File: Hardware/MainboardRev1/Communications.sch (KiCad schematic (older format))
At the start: 12 parts, among them J8 915MHz_SMA, U17 ublox_max-m8q, U18 RFM69HCW

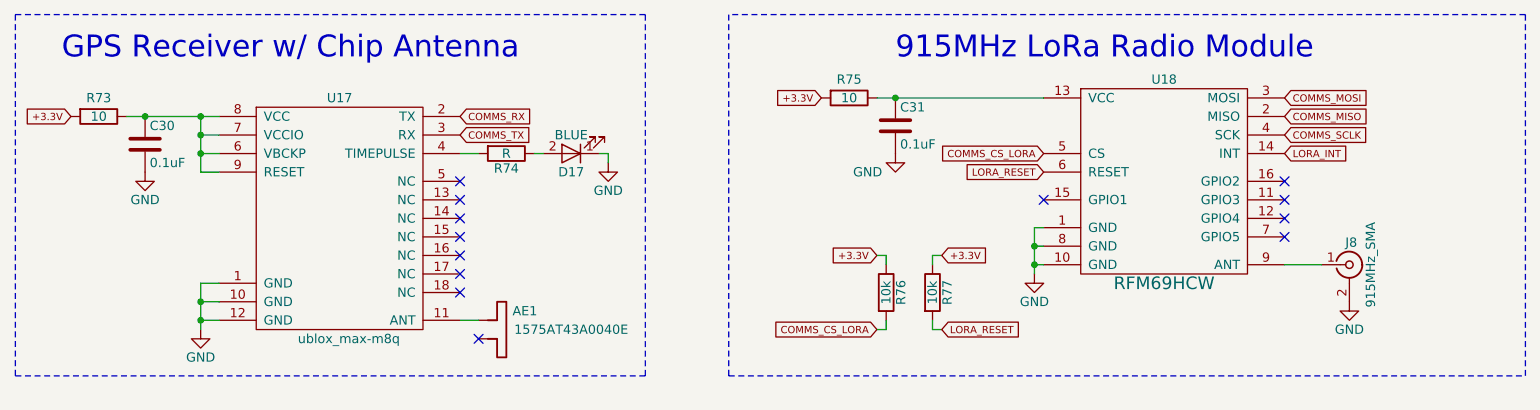
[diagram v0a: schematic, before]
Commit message: Small changes to schematic: Added voltage dividers for analog inputs, small net changes. Added footprints for each part
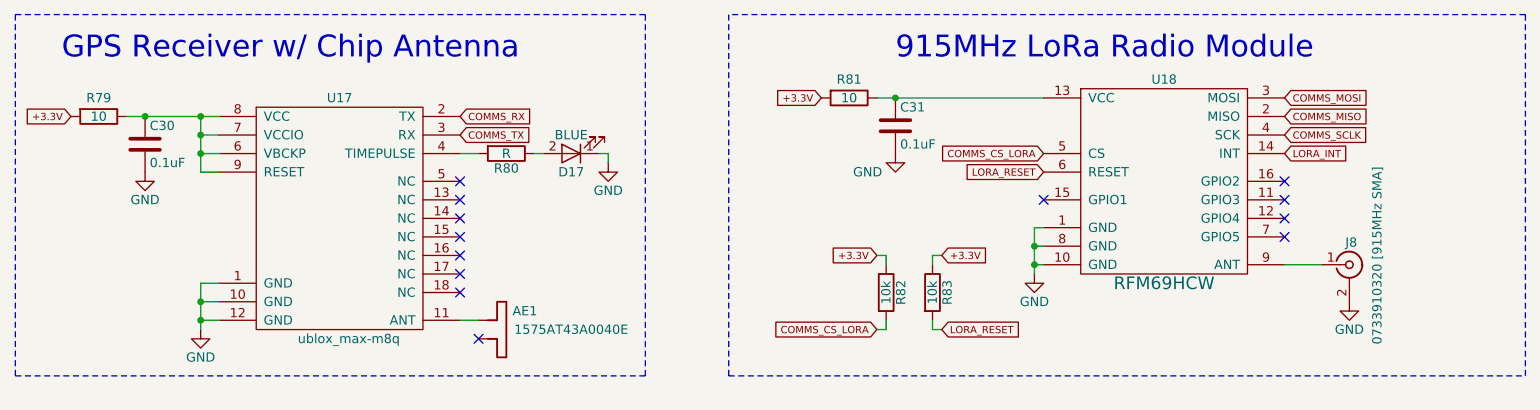
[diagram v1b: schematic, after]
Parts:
- AE1: footprint (none) -> Dans_Parts:ANT_CHIP_OMNI_1575MHz_GPS
- C30, C31: footprint (none) -> Capacitors_SMD:C_0603_HandSoldering
- D17: footprint (none) -> LEDs:LED_0603_HandSoldering
- J8: value 915MHz_SMA -> 0733910320 [915MHz SMA]; footprint (none) -> Dans_Parts:CONN_RP-SMA_Right_Angle_0733910320
- R79: renamed from R73; footprint (none) -> Resistors_SMD:R_0603_HandSoldering
- R80: renamed from R74; footprint (none) -> Resistors_SMD:R_0603_HandSoldering
- R81: renamed from R75; footprint (none) -> Resistors_SMD:R_0603_HandSoldering
- R82: renamed from R76; footprint (none) -> Resistors_SMD:R_0603_HandSoldering
- R83: renamed from R77; footprint (none) -> Resistors_SMD:R_0603_HandSoldering
- U17: footprint (none) -> _sensors:MAX-M8
- U18: footprint (none) -> SparkFun-RF:RFM69HCW-XXXS2
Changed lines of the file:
@@
 F 0 "U17" H 2600 2800 50  0000 C CNN
 F 1 "ublox_max-m8q" H 2650 1500 50  0000 C CNN
-F 2 "" H 2600 2100 118 0001 C CNN
+F 2 "_sensors:MAX-M8" H 2600 2100 118 0001 C CNN
 F 3 "" H 2600 2100 118 0001 C CNN
 	1    2600 2100
@@
 $EndComp
 $Comp
-L GND #PWR064
+L GND #PWR066
 U 1 1 5AFC74AD
 P 1850 2650
-F 0 "#PWR064" H 1850 2400 50  0001 C CNN
+F 0 "#PWR066" H 1850 2400 50  0001 C CNN
 F 1 "GND" H 1850 2500 50  0000 C CNN
 F 2 "" H 1850 2650 50  0001 C CNN
@@
 F 0 "C30" H 1575 1750 50  0000 L CNN
 F 1 "0.1uF" H 1575 1550 50  0000 L CNN
-F 2 "" H 1588 1500 50  0001 C CNN
+F 2 "Capacitors_SMD:C_0603_HandSoldering" H 1588 1500 50  0001 C CNN
 F 3 "" H 1550 1650 50  0001 C CNN
 	1    1550 1650
@@
 $EndComp
 $Comp
-L GND #PWR065
+L GND #PWR067
 U 1 1 5AFC7555
 P 1550 1800
-F 0 "#PWR065" H 1550 1550 50  0001 C CNN
+F 0 "#PWR067" H 1550 1550 50  0001 C CNN
 F 1 "GND" H 1550 1650 50  0000 C CNN
 F 2 "" H 1550 1800 50  0001 C CNN
@@
 +3.3V
 $Comp
-L R R73
+L R R79
 U 1 1 5AFC7789
 P 1300 1500
-F 0 "R73" V 1200 1500 50  0000 C CNN
+F 0 "R79" V 1200 1500 50  0000 C CNN
 F 1 "10" V 1300 1500 50  0000 C CNN
-F 2 "" V 1230 1500 50  0001 C CNN
+F 2 "Resistors_SMD:R_0603_HandSoldering" V 1230 1500 50  0001 C CNN
 F 3 "" H 1300 1500 50  0001 C CNN
 	1    1300 1500
@@
 F 0 "AE1" V 3500 2650 50  0000 C CNN
 F 1 "1575AT43A0040E" V 3600 2900 50  0000 C CNN
-F 2 "" H 3550 2600 50  0001 C CNN
+F 2 "Dans_Parts:ANT_CHIP_OMNI_1575MHz_GPS" H 3550 2600 50  0001 C CNN
 F 3 "" H 3550 2600 50  0001 C CNN
 	1    3550 2600
@@
 F 0 "C31" H 5625 1650 50  0000 L CNN
 F 1 "0.1uF" H 5625 1450 50  0000 L CNN
-F 2 "" H 5638 1400 50  0001 C CNN
+F 2 "Capacitors_SMD:C_0603_HandSoldering" H 5638 1400 50  0001 C CNN
 F 3 "" H 5600 1550 50  0001 C CNN
 	1    5600 1550
@@
 $EndComp
 $Comp
-L GND #PWR066
+L GND #PWR068
 U 1 1 5AFC9387
 P 5600 1700
-F 0 "#PWR066" H 5600 1450 50  0001 C CNN
+F 0 "#PWR068" H 5600 1450 50  0001 C CNN
 F 1 "GND" H 5450 1600 50  0000 C CNN
 F 2 "" H 5600 1700 50  0001 C CNN
@@
 $EndComp
 $Comp
-L R R75
+L R R81
 U 1 1 5AFC93C3
 P 5350 1400
-F 0 "R75" V 5250 1400 50  0000 C CNN
+F 0 "R81" V 5250 1400 50  0000 C CNN
 F 1 "10" V 5350 1400 50  0000 C CNN
-F 2 "" V 5280 1400 50  0001 C CNN
+F 2 "Resistors_SMD:R_0603_HandSoldering" V 5280 1400 50  0001 C CNN
 F 3 "" H 5350 1400 50  0001 C CNN
 	1    5350 1400
@@
 +3.3V
 $Comp
-L RFM69HCW U18
-U 1 1 5AFC98DB
-P 7050 1800
-F 0 "U18" H 7050 2300 50  0000 C CNN
-F 1 "RFM69HCW" H 7050 1200 68  0000 C CNN
-F 2 "" H 7050 1800 118 0001 C CNN
-F 3 "" H 7050 1800 118 0001 C CNN
-	1    7050 1800
-	1    0    0    -1
-$EndComp
-$Comp
-L GND #PWR067
+L GND #PWR069
 U 1 1 5AFC9C0E
 P 6350 2350
-F 0 "#PWR067" H 6350 2100 50  0001 C CNN
+F 0 "#PWR069" H 6350 2100 50  0001 C CNN
 F 1 "GND" H 6350 2200 50  0000 C CNN
 F 2 "" H 6350 2350 50  0001 C CNN
@@
 $EndComp
 $Comp
-L R R76
+L R R82
 U 1 1 5AFC9F45
 P 5550 2450
-F 0 "R76" V 5630 2450 50  0000 C CNN
+F 0 "R82" V 5630 2450 50  0000 C CNN
 F 1 "10k" V 5550 2450 50  0000 C CNN
-F 2 "" V 5480 2450 50  0001 C CNN
+F 2 "Resistors_SMD:R_0603_HandSoldering" V 5480 2450 50  0001 C CNN
 F 3 "" H 5550 2450 50  0001 C CNN
 	1    5550 2450
@@
 $EndComp
 $Comp
-L R R77
+L R R83
 U 1 1 5AFC9FBB
 P 5800 2450
-F 0 "R77" V 5880 2450 50  0000 C CNN
+F 0 "R83" V 5880 2450 50  0000 C CNN
 F 1 "10k" V 5800 2450 50  0000 C CNN
-F 2 "" V 5730 2450 50  0001 C CNN
+F 2 "Resistors_SMD:R_0603_HandSoldering" V 5730 2450 50  0001 C CNN
 F 3 "" H 5800 2450 50  0001 C CNN
 	1    5800 2450
@@
 P 8050 2300
 F 0 "J8" H 8060 2420 50  0000 C CNN
-F 1 "915MHz_SMA" V 8165 2300 50  0000 C CNN
-F 2 "" H 8050 2300 50  0001 C CNN
+F 1 "0733910320 [915MHz SMA]" V 8200 2350 50  0000 C CNN
+F 2 "Dans_Parts:CONN_RP-SMA_Right_Angle_0733910320" H 8050 2300 50  0001 C CNN
 F 3 "" H 8050 2300 50  0001 C CNN
 	1    8050 2300
@@
 $EndComp
 $Comp
-L GND #PWR068
+L GND #PWR070
 U 1 1 5AFCBF0B
 P 8050 2500
-F 0 "#PWR068" H 8050 2250 50  0001 C CNN
+F 0 "#PWR070" H 8050 2250 50  0001 C CNN
 F 1 "GND" H 8050 2350 50  0000 C CNN
 F 2 "" H 8050 2500 50  0001 C CNN
@@
 F 0 "D17" H 3850 1800 50  0000 C CNN
 F 1 "BLUE" H 3850 1600 50  0000 C CNN
-F 2 "" H 3850 1700 50  0001 C CNN
+F 2 "LEDs:LED_0603_HandSoldering" H 3850 1700 50  0001 C CNN
 F 3 "" H 3850 1700 50  0001 C CNN
 	1    3850 1700
@@
 	7900 2300 7700 2300
 $Comp
-L R R74
+L R R80
 U 1 1 5AFF29E0
 P 3500 1700
-F 0 "R74" V 3580 1700 50  0000 C CNN
+F 0 "R80" V 3580 1700 50  0000 C CNN
 F 1 "R" V 3500 1700 50  0000 C CNN
-F 2 "" V 3430 1700 50  0001 C CNN
+F 2 "Resistors_SMD:R_0603_HandSoldering" V 3430 1700 50  0001 C CNN
 F 3 "" H 3500 1700 50  0001 C CNN
 	1    3500 1700
@@
 	3700 1700 3650 1700
 $Comp
-L GND #PWR069
+L GND #PWR071
 U 1 1 5AFF2B6C
 P 4050 1750
-F 0 "#PWR069" H 4050 1500 50  0001 C CNN
+F 0 "#PWR071" H 4050 1500 50  0001 C CNN
 F 1 "GND" H 4050 1600 50  0000 C CNN
 F 2 "" H 4050 1750 50  0001 C CNN
@@
 Wire Wire Line
 	4050 1700 4000 1700
+$Comp
+L RFM69HCW U18
+U 1 1 5AFC3AD7
+P 7050 1800
+F 0 "U18" H 7050 2300 50  0000 C CNN
+F 1 "RFM69HCW" H 7050 1200 68  0000 C CNN
+F 2 "SparkFun-RF:RFM69HCW-XXXS2" H 7050 1800 118 0001 C CNN
+F 3 "" H 7050 1800 118 0001 C CNN
+	1    7050 1800
+	1    0    0    -1
+$EndComp
 $EndSCHEMATC

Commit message: Components placed. Needs to be routed.
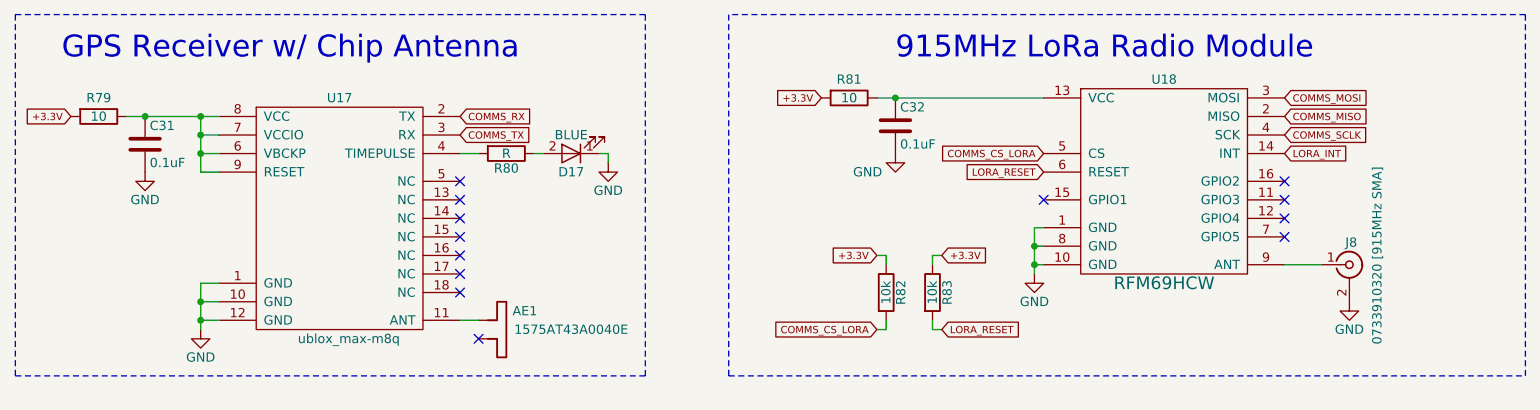
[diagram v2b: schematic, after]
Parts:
- renumbered C30 to C31, C31 to C32
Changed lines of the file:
@@
 LIBS:teensy3_6-OuterHeadersOnly
 LIBS:switches
+LIBS:mounting_hole_eighth_inch
 LIBS:MainboardRev1-cache
 EELAYER 25 0
@@
 $EndComp
 $Comp
-L GND #PWR066
+L GND #PWR072
 U 1 1 5AFC74AD
 P 1850 2650
-F 0 "#PWR066" H 1850 2400 50  0001 C CNN
+F 0 "#PWR072" H 1850 2400 50  0001 C CNN
 F 1 "GND" H 1850 2500 50  0000 C CNN
 F 2 "" H 1850 2650 50  0001 C CNN
@@
 $EndComp
 $Comp
-L C C30
+L C C31
 U 1 1 5AFC750B
 P 1550 1650
-F 0 "C30" H 1575 1750 50  0000 L CNN
+F 0 "C31" H 1575 1750 50  0000 L CNN
 F 1 "0.1uF" H 1575 1550 50  0000 L CNN
 F 2 "Capacitors_SMD:C_0603_HandSoldering" H 1588 1500 50  0001 C CNN
@@
 $EndComp
 $Comp
-L GND #PWR067
+L GND #PWR073
 U 1 1 5AFC7555
 P 1550 1800
-F 0 "#PWR067" H 1550 1550 50  0001 C CNN
+F 0 "#PWR073" H 1550 1550 50  0001 C CNN
 F 1 "GND" H 1550 1650 50  0000 C CNN
 F 2 "" H 1550 1800 50  0001 C CNN
@@
 GPS Receiver w/ Chip Antenna
 $Comp
-L C C31
+L C C32
 U 1 1 5AFC930D
 P 5600 1550
-F 0 "C31" H 5625 1650 50  0000 L CNN
+F 0 "C32" H 5625 1650 50  0000 L CNN
 F 1 "0.1uF" H 5625 1450 50  0000 L CNN
 F 2 "Capacitors_SMD:C_0603_HandSoldering" H 5638 1400 50  0001 C CNN
@@
 $EndComp
 $Comp
-L GND #PWR068
+L GND #PWR074
 U 1 1 5AFC9387
 P 5600 1700
-F 0 "#PWR068" H 5600 1450 50  0001 C CNN
+F 0 "#PWR074" H 5600 1450 50  0001 C CNN
 F 1 "GND" H 5450 1600 50  0000 C CNN
 F 2 "" H 5600 1700 50  0001 C CNN
@@
 +3.3V
 $Comp
-L GND #PWR069
+L GND #PWR075
 U 1 1 5AFC9C0E
 P 6350 2350
-F 0 "#PWR069" H 6350 2100 50  0001 C CNN
+F 0 "#PWR075" H 6350 2100 50  0001 C CNN
 F 1 "GND" H 6350 2200 50  0000 C CNN
 F 2 "" H 6350 2350 50  0001 C CNN
@@
 $EndComp
 $Comp
-L GND #PWR070
+L GND #PWR076
 U 1 1 5AFCBF0B
 P 8050 2500
-F 0 "#PWR070" H 8050 2250 50  0001 C CNN
+F 0 "#PWR076" H 8050 2250 50  0001 C CNN
 F 1 "GND" H 8050 2350 50  0000 C CNN
 F 2 "" H 8050 2500 50  0001 C CNN
@@
 	3700 1700 3650 1700
 $Comp
-L GND #PWR071
+L GND #PWR077
 U 1 1 5AFF2B6C
 P 4050 1750
-F 0 "#PWR071" H 4050 1500 50  0001 C CNN
+F 0 "#PWR077" H 4050 1500 50  0001 C CNN
 F 1 "GND" H 4050 1600 50  0000 C CNN
 F 2 "" H 4050 1750 50  0001 C CNN

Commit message: Added buzzer and strobe LED. Created BOM. Reannotated. Added sponsors to silkscreen. Needs to be routed and sent out. Good luck Matt!
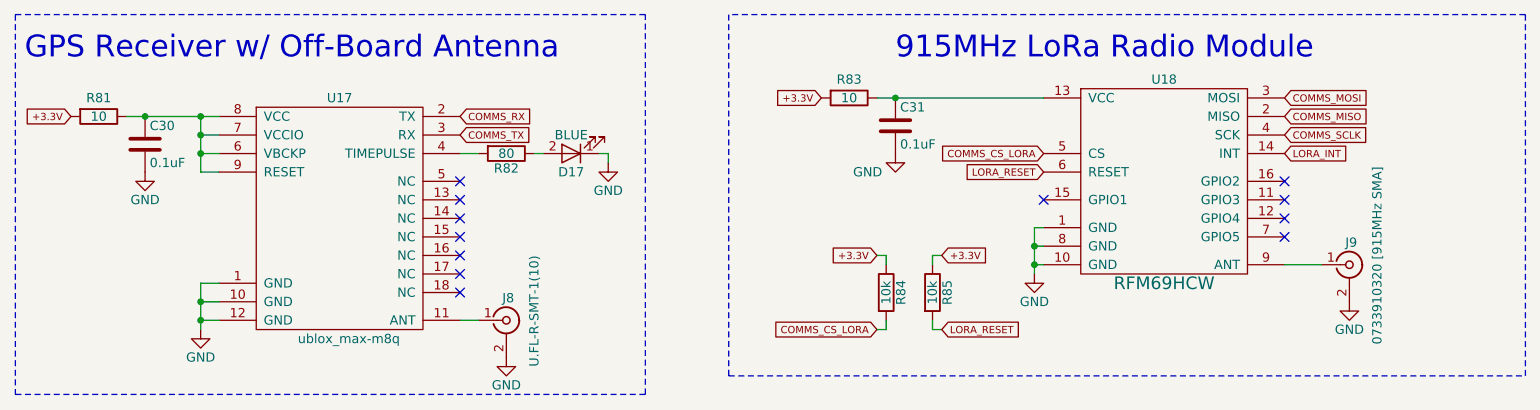
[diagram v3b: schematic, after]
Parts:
- removed AE1: 1575AT43A0040E, Dans_Parts:ANT_CHIP_OMNI_1575MHz_GPS, symbol Antenna_Dipole
- added J8: U.FL-R-SMT-1(10), Dans_Parts:HRS_U.FL-R-SMT-1(10), symbol CONN_COAXIAL
- R82: renamed from R80; value R -> 80
- renumbered C31 to C30, C32 to C31, J8 to J9, R79 to R81, R81 to R83, R82 to R84, R83 to R85
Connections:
- net GND: now also J8.2 (Ext)
- net at U17.11 (ANT): now also J8.1 (In)
- no-connect marks 13 -> 12
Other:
- note added: "GPS Receiver w/ Off-Board Antenna"
- note removed: "GPS Receiver w/ Chip Antenna"
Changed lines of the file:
@@
 $EndComp
 $Comp
-L GND #PWR072
+L GND #PWR070
 U 1 1 5AFC74AD
 P 1850 2650
-F 0 "#PWR072" H 1850 2400 50  0001 C CNN
+F 0 "#PWR070" H 1850 2400 50  0001 C CNN
 F 1 "GND" H 1850 2500 50  0000 C CNN
 F 2 "" H 1850 2650 50  0001 C CNN
@@
 $EndComp
 $Comp
-L C C31
+L C C30
 U 1 1 5AFC750B
 P 1550 1650
-F 0 "C31" H 1575 1750 50  0000 L CNN
+F 0 "C30" H 1575 1750 50  0000 L CNN
 F 1 "0.1uF" H 1575 1550 50  0000 L CNN
 F 2 "Capacitors_SMD:C_0603_HandSoldering" H 1588 1500 50  0001 C CNN
@@
 $EndComp
 $Comp
-L GND #PWR073
+L GND #PWR071
 U 1 1 5AFC7555
 P 1550 1800
-F 0 "#PWR073" H 1550 1550 50  0001 C CNN
+F 0 "#PWR071" H 1550 1550 50  0001 C CNN
 F 1 "GND" H 1550 1650 50  0000 C CNN
 F 2 "" H 1550 1800 50  0001 C CNN
@@
 +3.3V
 $Comp
-L R R79
+L R R81
 U 1 1 5AFC7789
 P 1300 1500
-F 0 "R79" V 1200 1500 50  0000 C CNN
+F 0 "R81" V 1200 1500 50  0000 C CNN
 F 1 "10" V 1300 1500 50  0000 C CNN
 F 2 "Resistors_SMD:R_0603_HandSoldering" V 1230 1500 50  0001 C CNN
@@
 NoConn ~ 3250 2350
 NoConn ~ 3250 2450
-$Comp
-L Antenna_Dipole AE1
-U 1 1 5AFC7D42
-P 3550 2600
-F 0 "AE1" V 3500 2650 50  0000 C CNN
-F 1 "1575AT43A0040E" V 3600 2900 50  0000 C CNN
-F 2 "Dans_Parts:ANT_CHIP_OMNI_1575MHz_GPS" H 3550 2600 50  0001 C CNN
-F 3 "" H 3550 2600 50  0001 C CNN
-	1    3550 2600
-	0    1    1    0
-$EndComp
-NoConn ~ 3350 2700
 Text GLabel 3250 1500 2    39   Input ~ 0
 COMMS_RX
 Text GLabel 3250 1600 2    39   Input ~ 0
 COMMS_TX
-Text Notes 1100 1200 0    118  ~ 0
-GPS Receiver w/ Chip Antenna
-$Comp
-L C C32
+Text Notes 900  1200 0    118  ~ 0
+GPS Receiver w/ Off-Board Antenna
+$Comp
+L C C31
 U 1 1 5AFC930D
 P 5600 1550
-F 0 "C32" H 5625 1650 50  0000 L CNN
+F 0 "C31" H 5625 1650 50  0000 L CNN
 F 1 "0.1uF" H 5625 1450 50  0000 L CNN
 F 2 "Capacitors_SMD:C_0603_HandSoldering" H 5638 1400 50  0001 C CNN
@@
 $EndComp
 $Comp
-L GND #PWR074
+L GND #PWR072
 U 1 1 5AFC9387
 P 5600 1700
-F 0 "#PWR074" H 5600 1450 50  0001 C CNN
+F 0 "#PWR072" H 5600 1450 50  0001 C CNN
 F 1 "GND" H 5450 1600 50  0000 C CNN
 F 2 "" H 5600 1700 50  0001 C CNN
@@
 $EndComp
 $Comp
-L R R81
+L R R83
 U 1 1 5AFC93C3
 P 5350 1400
-F 0 "R81" V 5250 1400 50  0000 C CNN
+F 0 "R83" V 5250 1400 50  0000 C CNN
 F 1 "10" V 5350 1400 50  0000 C CNN
 F 2 "Resistors_SMD:R_0603_HandSoldering" V 5280 1400 50  0001 C CNN
@@
 +3.3V
 $Comp
-L GND #PWR075
+L GND #PWR073
 U 1 1 5AFC9C0E
 P 6350 2350
-F 0 "#PWR075" H 6350 2100 50  0001 C CNN
+F 0 "#PWR073" H 6350 2100 50  0001 C CNN
 F 1 "GND" H 6350 2200 50  0000 C CNN
 F 2 "" H 6350 2350 50  0001 C CNN
@@
 $EndComp
 $Comp
-L R R82
+L R R84
 U 1 1 5AFC9F45
 P 5550 2450
-F 0 "R82" V 5630 2450 50  0000 C CNN
+F 0 "R84" V 5630 2450 50  0000 C CNN
 F 1 "10k" V 5550 2450 50  0000 C CNN
 F 2 "Resistors_SMD:R_0603_HandSoldering" V 5480 2450 50  0001 C CNN
@@
 $EndComp
 $Comp
-L R R83
+L R R85
 U 1 1 5AFC9FBB
 P 5800 2450
-F 0 "R83" V 5880 2450 50  0000 C CNN
+F 0 "R85" V 5880 2450 50  0000 C CNN
 F 1 "10k" V 5800 2450 50  0000 C CNN
 F 2 "Resistors_SMD:R_0603_HandSoldering" V 5730 2450 50  0001 C CNN
@@
 915MHz LoRa Radio Module
 $Comp
-L CONN_COAXIAL J8
+L CONN_COAXIAL J9
 U 1 1 5AFCBDEA
 P 8050 2300
-F 0 "J8" H 8060 2420 50  0000 C CNN
+F 0 "J9" H 8060 2420 50  0000 C CNN
 F 1 "0733910320 [915MHz SMA]" V 8200 2350 50  0000 C CNN
 F 2 "Dans_Parts:CONN_RP-SMA_Right_Angle_0733910320" H 8050 2300 50  0001 C CNN
@@
 $EndComp
 $Comp
-L GND #PWR076
+L GND #PWR074
 U 1 1 5AFCBF0B
 P 8050 2500
-F 0 "#PWR076" H 8050 2250 50  0001 C CNN
+F 0 "#PWR074" H 8050 2250 50  0001 C CNN
 F 1 "GND" H 8050 2350 50  0000 C CNN
 F 2 "" H 8050 2500 50  0001 C CNN
@@
 	3350 2600 3250 2600
 Wire Notes Line
-	850  950  850  2900
-Wire Notes Line
-	850  2900 4250 2900
-Wire Notes Line
-	4250 2900 4250 950
+	850  950  850  3000
+Wire Notes Line
+	850  3000 4250 3000
+Wire Notes Line
+	4250 3000 4250 950
 Wire Notes Line
 	4250 950  850  950
 Connection ~ 5600 1400
 Wire Wire Line
-	6350 2350 6350 2100
+	6350 2100 6350 2350
 Wire Wire Line
 	6350 2100 6400 2100
@@
 	7900 2300 7700 2300
 $Comp
-L R R80
+L R R82
 U 1 1 5AFF29E0
 P 3500 1700
-F 0 "R80" V 3580 1700 50  0000 C CNN
-F 1 "R" V 3500 1700 50  0000 C CNN
+F 0 "R82" V 3580 1700 50  0000 C CNN
+F 1 "80" V 3500 1700 50  0000 C CNN
 F 2 "Resistors_SMD:R_0603_HandSoldering" V 3430 1700 50  0001 C CNN
 F 3 "" H 3500 1700 50  0001 C CNN
@@
 	3700 1700 3650 1700
 $Comp
-L GND #PWR077
+L GND #PWR075
 U 1 1 5AFF2B6C
 P 4050 1750
-F 0 "#PWR077" H 4050 1500 50  0001 C CNN
+F 0 "#PWR075" H 4050 1500 50  0001 C CNN
 F 1 "GND" H 4050 1600 50  0000 C CNN
 F 2 "" H 4050 1750 50  0001 C CNN
@@
 	1    0    0    -1
 $EndComp
+$Comp
+L CONN_COAXIAL J8
+U 1 1 5B050156
+P 3500 2600
+F 0 "J8" H 3510 2720 50  0000 C CNN
+F 1 "U.FL-R-SMT-1(10)" V 3650 2650 50  0000 C CNN
+F 2 "Dans_Parts:HRS_U.FL-R-SMT-1(10)" H 3500 2600 50  0001 C CNN
+F 3 "" H 3500 2600 50  0001 C CNN
+	1    3500 2600
+	1    0    0    -1
+$EndComp
+$Comp
+L GND #PWR076
+U 1 1 5B050256
+P 3500 2800
+F 0 "#PWR076" H 3500 2550 50  0001 C CNN
+F 1 "GND" H 3500 2650 50  0000 C CNN
+F 2 "" H 3500 2800 50  0001 C CNN
+F 3 "" H 3500 2800 50  0001 C CNN
+	1    3500 2800
+	1    0    0    -1
+$EndComp
